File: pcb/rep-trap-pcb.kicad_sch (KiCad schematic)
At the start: 0 parts

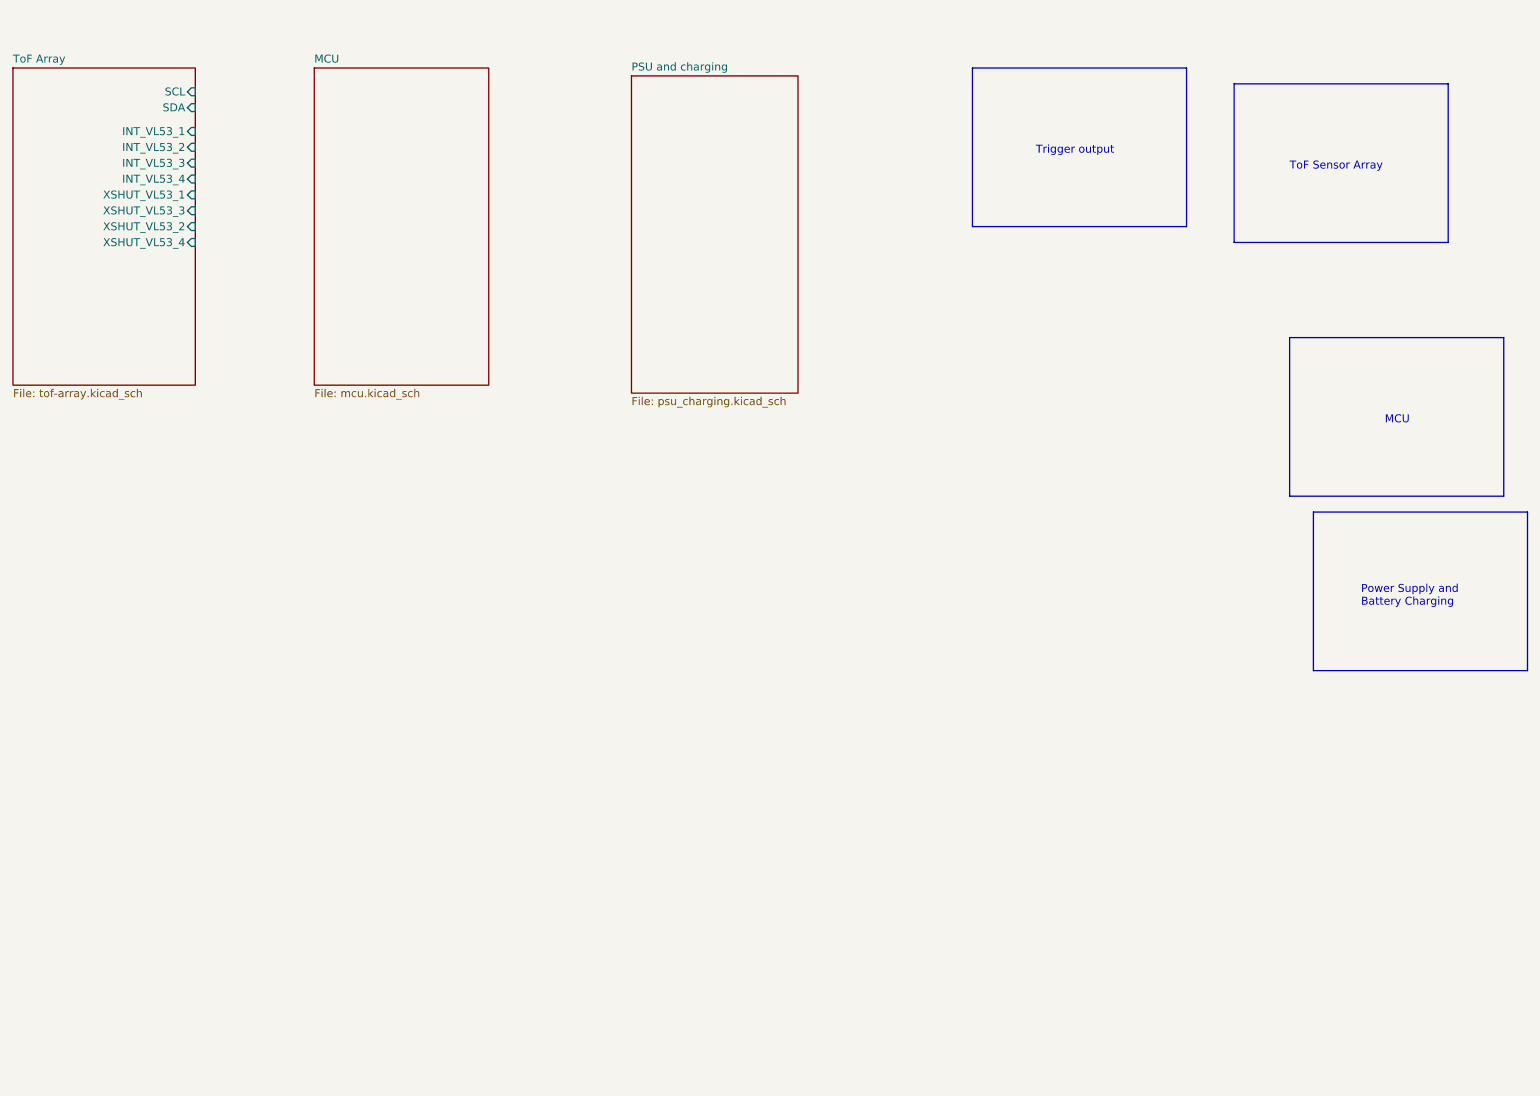
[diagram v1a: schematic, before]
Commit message: Added pcb design for first prototype
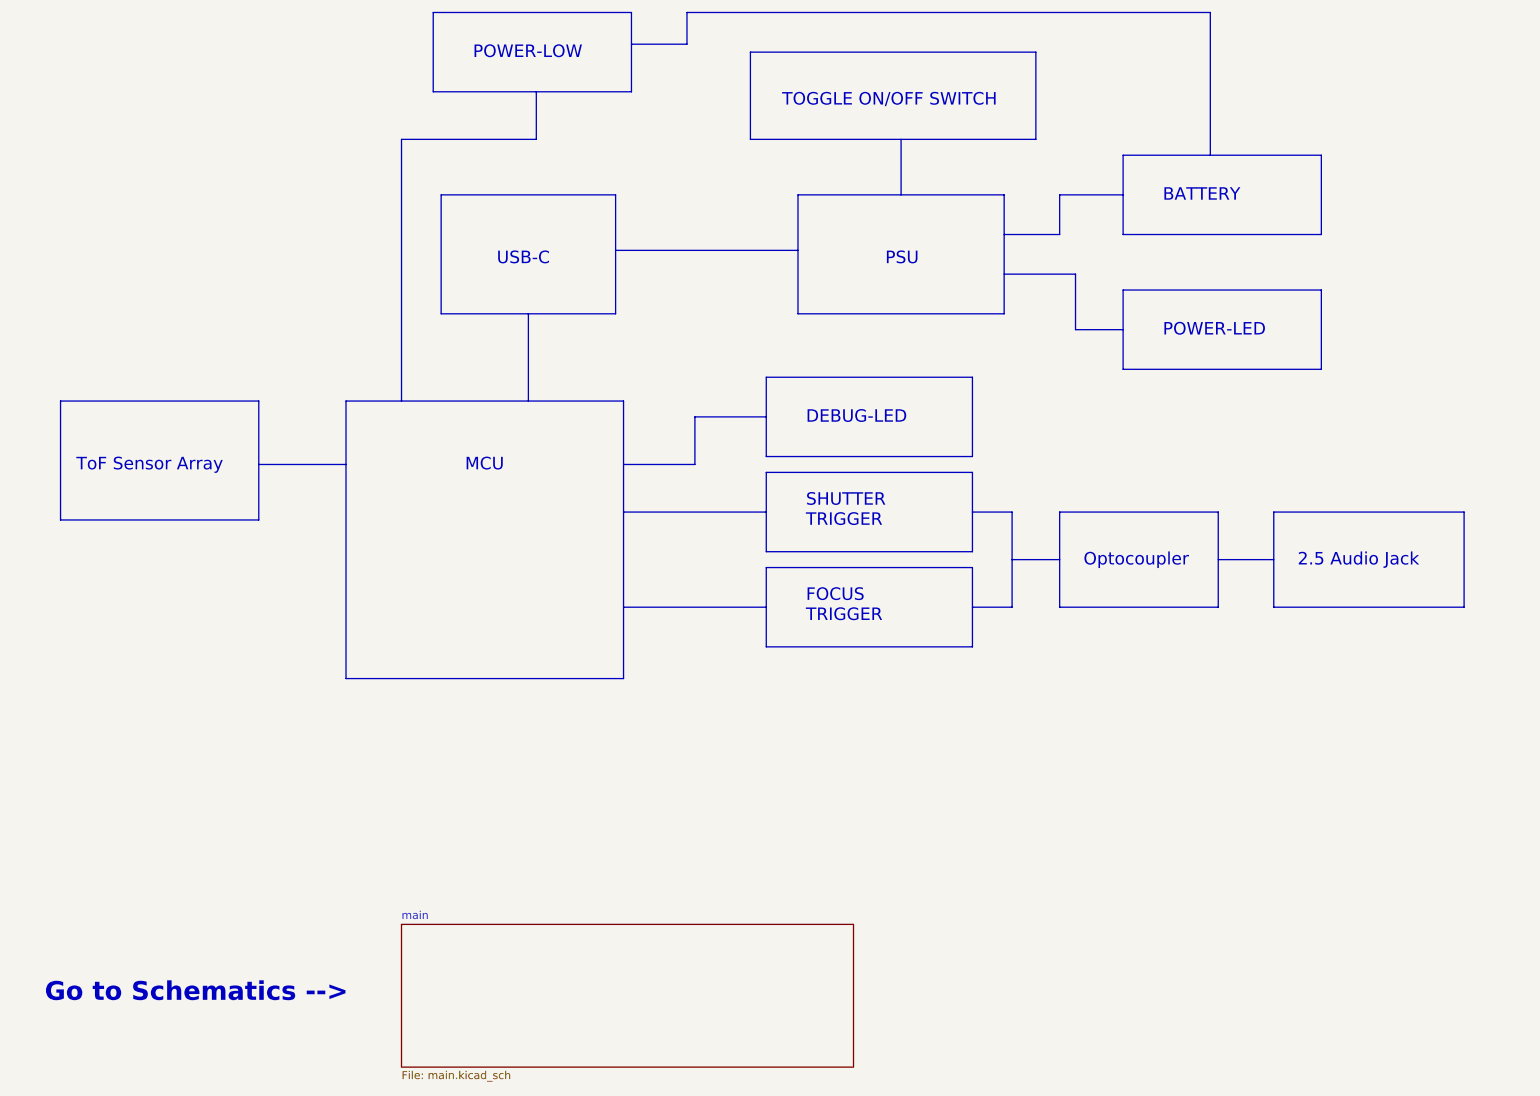
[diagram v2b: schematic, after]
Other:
- removed sheet MCU
- removed sheet PSU and charging
- removed sheet ToF Array
- added sheet main (main.kicad_sch)
- note added: "2.5 Audio Jack"
- note added: "BATTERY"
- note added: "DEBUG-LED"
- note added: "FOCUS TRIGGER"
- note added: "Go to Schematics -->"
- note added: "Optocoupler"
- note added: "POWER-LED"
- note added: "POWER-LOW"
- note added: "PSU"
- note added: "SHUTTER TRIGGER"
- note added: "TOGGLE ON/OFF SWITCH"
- note added: "USB-C"
- note removed: "Power Supply and Battery Charging"
- note removed: "Trigger output"
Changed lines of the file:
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@@
     (company "open-things")
   )
-  (rectangle (start 240.03 101.6) (end 274.32 127)
+  (polyline (pts (xy 93.98 41.91) (xy 115.57 41.91))
+    (stroke (width 0) (type default))
+  )
+  (polyline (pts (xy 139.7 21.59) (xy 223.52 21.59))
+    (stroke (width 0) (type default))
+  )
+  (polyline (pts (xy 173.99 41.91) (xy 173.99 50.8))
+    (stroke (width 0) (type default))
+  )
+  (polyline (pts (xy 185.42 101.6) (xy 191.77 101.6))
+    (stroke (width 0) (type default))
+  )
+  (polyline (pts (xy 190.5 57.15) (xy 199.39 57.15))
+    (stroke (width 0) (type default))
+  )
+  (polyline (pts (xy 130.81 26.67) (xy 139.7 26.67))
+    (stroke (width 0) (type default))
+  )
+  (polyline (pts (xy 129.54 93.98) (xy 140.97 93.98))
+    (stroke (width 0) (type default))
+  )
+  (polyline (pts (xy 114.3 69.85) (xy 114.3 83.82))
+    (stroke (width 0) (type default))
+  )
+  (polyline (pts (xy 190.5 63.5) (xy 201.93 63.5))
+    (stroke (width 0) (type default))
+  )
+  (polyline (pts (xy 129.54 101.6) (xy 152.4 101.6))
+    (stroke (width 0) (type default))
+  )
+  (polyline (pts (xy 129.54 116.84) (xy 152.4 116.84))
+    (stroke (width 0) (type default))
+  )
+  (polyline (pts (xy 201.93 72.39) (xy 201.93 63.5))
+    (stroke (width 0) (type default))
+  )
+  (polyline (pts (xy 199.39 50.8) (xy 199.39 57.15))
+    (stroke (width 0) (type default))
+  )
+  (polyline (pts (xy 128.27 59.69) (xy 157.48 59.69))
+    (stroke (width 0) (type default))
+  )
+  (polyline (pts (xy 93.98 83.82) (xy 93.98 41.91))
+    (stroke (width 0) (type default))
+  )
+  (polyline (pts (xy 224.79 109.22) (xy 233.68 109.22))
+    (stroke (width 0) (type default))
+  )
+  (polyline (pts (xy 199.39 109.22) (xy 191.77 109.22))
+    (stroke (width 0) (type default))
+  )
+  (polyline (pts (xy 185.42 116.84) (xy 191.77 116.84))
+    (stroke (width 0) (type default))
+  )
+  (polyline (pts (xy 191.77 109.22) (xy 191.77 116.84))
+    (stroke (width 0) (type default))
+  )
+  (polyline (pts (xy 139.7 26.67) (xy 139.7 21.59))
+    (stroke (width 0) (type default))
+  )
+  (polyline (pts (xy 71.12 93.98) (xy 85.09 93.98))
+    (stroke (width 0) (type default))
+  )
+  (polyline (pts (xy 209.55 50.8) (xy 199.39 50.8))
+    (stroke (width 0) (type default))
+  )
+  (polyline (pts (xy 115.57 34.29) (xy 115.57 41.91))
+    (stroke (width 0) (type default))
+  )
+  (polyline (pts (xy 152.4 86.36) (xy 140.97 86.36))
+    (stroke (width 0) (type default))
+  )
+  (polyline (pts (xy 191.77 109.22) (xy 191.77 101.6))
+    (stroke (width 0) (type default))
+  )
+  (polyline (pts (xy 223.52 21.59) (xy 223.52 44.45))
+    (stroke (width 0) (type default))
+  )
+  (polyline (pts (xy 140.97 86.36) (xy 140.97 93.98))
+    (stroke (width 0) (type default))
+  )
+  (polyline (pts (xy 209.55 72.39) (xy 201.93 72.39))
+    (stroke (width 0) (type default))
+  )
+  (rectangle (start 233.68 101.6) (end 264.16 116.84)
     (stroke (width 0) (type default))
     (fill (type none))
   )
-  (rectangle (start 185.42 30.48) (end 219.71 55.88)
+  (rectangle (start 39.37 83.82) (end 71.12 102.87)
     (stroke (width 0) (type default))
     (fill (type none))
   )
-  (rectangle (start 236.22 73.66) (end 270.51 99.06)
+  (rectangle (start 99.06 21.59) (end 130.81 34.29)
     (stroke (width 0) (type default))
     (fill (type none))
   )
-  (rectangle (start 227.33 33.02) (end 261.62 58.42)
+  (rectangle (start 152.4 95.25) (end 185.42 107.95)
     (stroke (width 0) (type default))
     (fill (type none))
   )
-  (text "Power Supply and \nBattery Charging" (at 247.65 116.84 0)
-    (effects (font (size 1.27 1.27)) (justify left bottom))
+  (rectangle (start 152.4 110.49) (end 185.42 123.19)
+    (stroke (width 0) (type default))
+    (fill (type none))
   )
-  (text "ToF Sensor Array" (at 236.22 46.99 0)
-    (effects (font (size 1.27 1.27)) (justify left bottom))
+  (rectangle (start 152.4 80.01) (end 185.42 92.71)
+    (stroke (width 0) (type default))
+    (fill (type none))
   )
-  (text "Trigger output" (at 195.58 44.45 0)
-    (effects (font (size 1.27 1.27)) (justify left bottom))
+  (rectangle (start 100.33 50.8) (end 128.27 69.85)
+    (stroke (width 0) (type default))
+    (fill (type none))
   )
-  (text "MCU" (at 251.46 87.63 0)
-    (effects (font (size 1.27 1.27)) (justify left bottom))
+  (rectangle (start 149.86 27.94) (end 195.58 41.91)
+    (stroke (width 0) (type default))
+    (fill (type none))
   )
-  (sheet (at 31.75 30.48) (size 29.21 50.8) (fields_autoplaced)
+  (rectangle (start 209.55 66.04) (end 241.3 78.74)
+    (stroke (width 0) (type default))
+    (fill (type none))
+  )
+  (rectangle (start 209.55 44.45) (end 241.3 57.15)
+    (stroke (width 0) (type default))
+    (fill (type none))
+  )
+  (rectangle (start 199.39 101.6) (end 224.79 116.84)
+    (stroke (width 0) (type default))
+    (fill (type none))
+  )
+  (rectangle (start 157.48 50.8) (end 190.5 69.85)
+    (stroke (width 0) (type default))
+    (fill (type none))
+  )
+  (rectangle (start 85.09 83.82) (end 129.54 128.27)
+    (stroke (width 0) (type default))
+    (fill (type none))
+  )
+  (text "ToF Sensor Array" (at 41.91 95.25 0)
+    (effects (font (size 2 2)) (justify left bottom))
+  )
+  (text "FOCUS\nTRIGGER" (at 158.75 119.38 0)
+    (effects (font (size 2 2)) (justify left bottom))
+  )
+  (text "TOGGLE ON/OFF SWITCH" (at 154.94 36.83 0)
+    (effects (font (size 2 2)) (justify left bottom))
+  )
+  (text "SHUTTER \nTRIGGER" (at 158.75 104.14 0)
+    (effects (font (size 2 2)) (justify left bottom))
+  )
+  (text "DEBUG-LED" (at 158.75 87.63 0)
+    (effects (font (size 2 2)) (justify left bottom))
+  )
+  (text "BATTERY" (at 215.9 52.07 0)
+    (effects (font (size 2 2)) (justify left bottom))
+  )
+  (text "USB-C\n" (at 109.22 62.23 0)
+    (effects (font (size 2 2)) (justify left bottom))
+  )
+  (text "MCU" (at 104.14 95.25 0)
+    (effects (font (size 2 2)) (justify left bottom))
+  )
+  (text "PSU" (at 171.45 62.23 0)
+    (effects (font (size 2 2)) (justify left bottom))
+  )
+  (text "POWER-LED" (at 215.9 73.66 0)
+    (effects (font (size 2 2)) (justify left bottom))
+  )
+  (text "Optocoupler" (at 203.2 110.49 0)
+    (effects (font (size 2 2)) (justify left bottom))
+  )
+  (text "POWER-LOW" (at 105.41 29.21 0)
+    (effects (font (size 2 2)) (justify left bottom))
+  )
+  (text "2.5 Audio Jack" (at 237.49 110.49 0)
+    (effects (font (size 2 2)) (justify left bottom))
+  )
+  (text "Go to Schematics -->" (at 36.83 180.34 0)
+    (effects (font (size 3 3) (thickness 0.6) bold) (justify left bottom))
+  )
+  (sheet (at 93.98 167.64) (size 72.39 22.86) (fields_autoplaced)
     (stroke (width 0.1524) (type solid))
     (fill (color 0 0 0 0.0000))
-    (property "Sheetname" "ToF Array" (at 31.75 29.7684 0)
+    (property "Sheetname" "main" (at 93.98 166.9284 0)
       (effects (font (size 1.27 1.27)) (justify left bottom))
     )
-    (property "Sheetfile" "tof-array.kicad_sch" (at 31.75 81.8646 0)
-      (effects (font (size 1.27 1.27)) (justify left top))
-    )
-    (pin "SCL" input (at 60.96 34.29 0)
-      (effects (font (size 1.27 1.27)) (justify right))
-    )
-    (pin "SDA" input (at 60.96 36.83 0)
-      (effects (font (size 1.27 1.27)) (justify right))
-    )
-    (pin "INT_VL53_1" input (at 60.96 40.64 0)
-      (effects (font (size 1.27 1.27)) (justify right))
-    )
-    (pin "INT_VL53_2" input (at 60.96 43.18 0)
-      (effects (font (size 1.27 1.27)) (justify right))
-    )
-    (pin "INT_VL53_3" input (at 60.96 45.72 0)
-      (effects (font (size 1.27 1.27)) (justify right))
-    )
-    (pin "INT_VL53_4" input (at 60.96 48.26 0)
-      (effects (font (size 1.27 1.27)) (justify right))
-    )
-    (pin "XSHUT_VL53_1" input (at 60.96 50.8 0)
-      (effects (font (size 1.27 1.27)) (justify right))
-    )
-    (pin "XSHUT_VL53_3" input (at 60.96 53.34 0)
-      (effects (font (size 1.27 1.27)) (justify right))
-    )
-    (pin "XSHUT_VL53_2" input (at 60.96 55.88 0)
-      (effects (font (size 1.27 1.27)) (justify right))
-    )
-    (pin "XSHUT_VL53_4" input (at 60.96 58.42 0)
-      (effects (font (size 1.27 1.27)) (justify right))
-    )
-    (instances
-      (project "rep-trap-pcb"
-        (path "/b363dc8f-4a45-4779-a397-ccb82393dab8" (page "2"))
-      )
-    )
-  )
-  (sheet (at 130.81 31.75) (size 26.67 50.8) (fields_autoplaced)
-    (stroke (width 0.1524) (type solid))
-    (fill (color 0 0 0 0.0000))
-    (property "Sheetname" "PSU and charging" (at 130.81 31.0384 0)
-      (effects (font (size 1.27 1.27)) (justify left bottom))
-    )
-    (property "Sheetfile" "psu_charging.kicad_sch" (at 130.81 83.1346 0)
+    (property "Sheetfile" "main.kicad_sch" (at 93.98 191.0846 0)
       (effects (font (size 1.27 1.27)) (justify left top))
     )
     (instances
       (project "rep-trap-pcb"
-        (path "/b363dc8f-4a45-4779-a397-ccb82393dab8" (page "4"))
+        (path "/b363dc8f-4a45-4779-a397-ccb82393dab8" (page "5"))
       )
     )
-  )
-  (sheet (at 80.01 30.48) (size 27.94 50.8) (fields_autoplaced)
-    (stroke (width 0.1524) (type solid))
-    (fill (color 0 0 0 0.0000))
-    (property "Sheetname" "MCU" (at 80.01 29.7684 0)
-      (effects (font (size 1.27 1.27)) (justify left bottom))
-    )
-    (property "Sheetfile" "mcu.kicad_sch" (at 80.01 81.8646 0)
-      (effects (font (size 1.27 1.27)) (justify left top))
-    )
-    (instances
-      (project "rep-trap-pcb"
-        (path "/b363dc8f-4a45-4779-a397-ccb82393dab8" (page "3"))
-      )
-    )

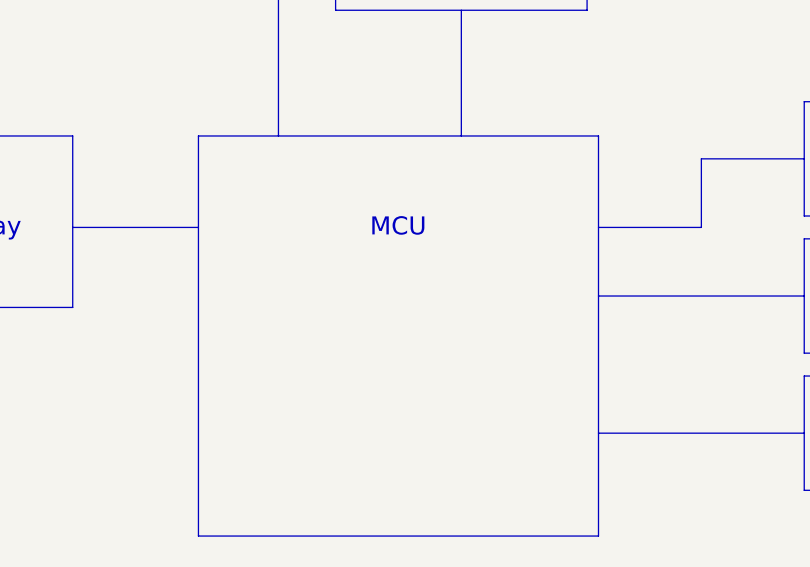
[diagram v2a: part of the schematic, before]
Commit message: Refactored details component namings + bom excludings
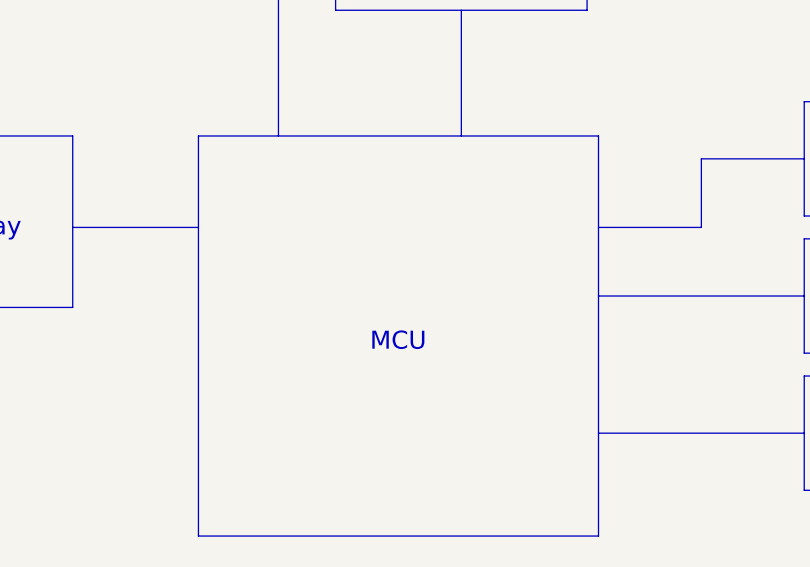
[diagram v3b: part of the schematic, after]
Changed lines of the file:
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@@
     (effects (font (size 2 2)) (justify left bottom))
   )
-  (text "MCU" (at 104.14 95.25 0)
+  (text "MCU" (at 104.14 107.95 0)
     (effects (font (size 2 2)) (justify left bottom))
   )
